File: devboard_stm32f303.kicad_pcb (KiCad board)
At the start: 2 copper layers, 50 x 17.8 mm, 20 parts, among them J2 USB_B_Mini, J3 Conn_01x20, J4 Conn_01x20, U1 STM32F303CCTx, U2 AMS1117-3.3, Y1 Crystal_Small

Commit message: More routing
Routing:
- net GND: track 45.2 -> 51.8 mm
- net +3V3: track 110.8 -> 117.0 mm
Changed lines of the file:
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@@
     (thickness 1.6)
     (drawings 9)
-    (tracks 194)
+    (tracks 202)
     (zones 0)
     (modules 20)
@@
   (segment (start 110.49 36.068) (end 107.315 32.893) (width 0.254) (layer B.Cu) (net 1))
   (segment (start 107.315 32.893) (end 107.331136 32.909136) (width 0.254) (layer B.Cu) (net 1))
+  (segment (start 97.0785 36.068) (end 97.566 36.068) (width 0.254) (layer F.Cu) (net 1))
+  (segment (start 96.498 36.068) (end 97.0785 36.068) (width 0.254) (layer F.Cu) (net 1))
+  (segment (start 93.091 32.661) (end 96.498 36.068) (width 0.254) (layer F.Cu) (net 1))
+  (segment (start 93.091 31.907) (end 93.091 32.661) (width 0.254) (layer F.Cu) (net 1))
   (segment (start 111.322 33.401) (end 112.649 33.401) (width 0.127) (layer F.Cu) (net 2))
   (segment (start 109.483675 35.239325) (end 111.322 33.401) (width 0.127) (layer F.Cu) (net 2))
@@
   (segment (start 96.266 32.193) (end 96.266 25.4) (width 0.254) (layer F.Cu) (net 4))
   (segment (start 96.266 25.4) (end 96.774 24.892) (width 0.254) (layer F.Cu) (net 4))
-  (segment (start 96.774 24.892) (end 99.314 24.892) (width 0.254) (layer F.Cu) (net 4))
   (segment (start 99.088628 24.893372) (end 99.314 24.892) (width 0.254) (layer F.Cu) (net 4))
   (segment (start 99.314 24.892) (end 113.539372 24.893372) (width 0.254) (layer F.Cu) (net 4))
@@
   (segment (start 111.76 27.686) (end 115.951 27.686) (width 0.254) (layer F.Cu) (net 4))
   (segment (start 116.205 27.432) (end 116.078 27.432) (width 0.254) (layer F.Cu) (net 4))
+  (segment (start 93.091 28.553) (end 96.752 24.892) (width 0.254) (layer F.Cu) (net 4))
+  (segment (start 93.091 29.307) (end 93.091 28.553) (width 0.254) (layer F.Cu) (net 4))
+  (segment (start 96.774 24.892) (end 97.028 24.892) (width 0.254) (layer F.Cu) (net 4))
+  (segment (start 96.752 24.892) (end 97.028 24.892) (width 0.254) (layer F.Cu) (net 4))
+  (segment (start 97.028 24.892) (end 99.314 24.892) (width 0.254) (layer F.Cu) (net 4))
   (via (at 108.458 35.802825) (size 0.6) (drill 0.3) (layers F.Cu B.Cu) (net 5))
   (segment (start 110.5685 36.068) (end 108.723175 36.068) (width 0.127) (layer F.Cu) (net 5))

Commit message: New board layout
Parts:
- C5: moved to F.Cu
- C8, D1, R2: moved to B.Cu
- moved C8 9.03 mm to (126.7, 26.2)
- moved C6 7.36 mm to (118.8, 37.1)
- moved R2 3.73 mm to (131.2, 30.2), turned to 0 degrees
- moved F1 3.37 mm to (131.2, 27.9), turned to 180 degrees
- moved J3 3.30 mm to (140.7, 20.3)
- moved D1 2.81 mm to (131.2, 32.5)
- moved C7 2.39 mm to (97.8, 24.1)
- moved C3 2.29 mm to (111.4, 24.1)
- moved J4 1.78 mm to (140.7, 40.6)
- moved C2 1.63 mm to (116.8, 28.8)
- moved C1 1.63 mm to (116.8, 32.4)
- moved Y1 1.62 mm to (113.9, 30.6)
- moved C9 0.91 mm to (126.7, 30.0), turned to 270 degrees
- moved U2 0.88 mm to (126.8, 30.0), turned to 180 degrees
- moved C4 0.85 mm to (98.1, 36.8)
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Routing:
- net +3V3: track 117.0 -> 0.00 mm, vias 3 -> 0
- net GND: track 51.8 -> 0.00 mm, vias 2 -> 0
- net D+: track 37.1 -> 0.00 mm, vias 4 -> 0
- net D-: track 35.6 -> 0.00 mm, vias 2 -> 0
- net OSC_OUT: track 12.8 -> 0.00 mm
- net OSC_IN: track 9.87 -> 0.00 mm
- net BOOT0: track 9.60 -> 0.00 mm, vias 3 -> 0
- net Net-(F1-Pad1): track 8.07 -> 0.00 mm, vias 1 -> 0
- net RESET: track 7.16 -> 0.00 mm, vias 2 -> 0
- net Net-(C8-Pad1): track 6.68 -> 0.00 mm
- net VBUS: track 3.11 -> 0.00 mm, vias 1 -> 0
- net Net-(JP1-Pad2): track 2.73 -> 0.00 mm, vias 1 -> 0
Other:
- board size 50 x 17.8 mm -> 51.1 x 22.4 mm
- net class Default: clearance 0.2 -> 0.127
- net class Power: clearance 0.2 -> 0.1905
- rule trace_clearance: 0.2 -> 0.127

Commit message: Basic routing
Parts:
- added D2: 1N5819, Diode_SMD:D_SOD-123, B.Cu at (137.8, 25.9)
- added SW1: SW_Push, Button_Switch_THT:SW_PUSH_6mm, F.Cu at (130.0, 37.0)
- C6: moved to B.Cu
- JP1: footprint Jumper:SolderJumper-3_P1.3mm_Open_Pad1.0x1.5mm -> Connector_PinHeader_2.54mm:PinHeader_1x03_P2.54mm_Vertical
- moved F1 9.21 mm to (140.1, 30.4), turned to 270 degrees
- moved D1 7.07 mm to (137.8, 35.1)
- moved C5 6.63 mm to (112.9, 30.4)
- moved C6 6.13 mm to (124.5, 34.7)
- moved C8 6.01 mm to (132.3, 24.0), turned to 270 degrees
- moved Y1 4.62 mm to (114.6, 35.1)
- moved C2 4.62 mm to (117.5, 33.4)
- moved C1 4.62 mm to (117.5, 37.0)
- moved U2 4.06 mm to (126.8, 25.9)
- moved C9 4.06 mm to (126.7, 25.9)
- moved JP1 3.18 mm to (93.2, 33.8), turned to 180 degrees
- moved R2 2.58 mm to (132.3, 27.9), turned to 270 degrees
- moved R1 0.76 mm to (96.3, 30.8)
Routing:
- net +3V3: track 0.00 -> 75.8 mm, vias 0 -> 4
- net D+: track 0.00 -> 56.5 mm
- net D-: track 0.00 -> 55.4 mm
- net GND: track 0.00 -> 30.1 mm, vias 0 -> 2
- net OSC_OUT: track 0.00 -> 13.7 mm
- net OSC_IN: track 0.00 -> 12.2 mm

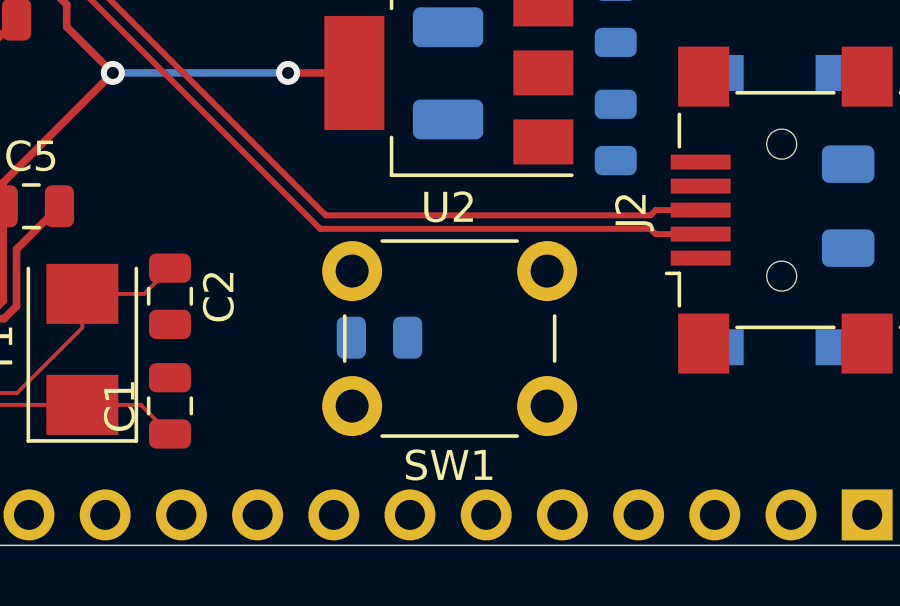
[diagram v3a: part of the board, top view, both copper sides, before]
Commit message: Autoroute rest of the board
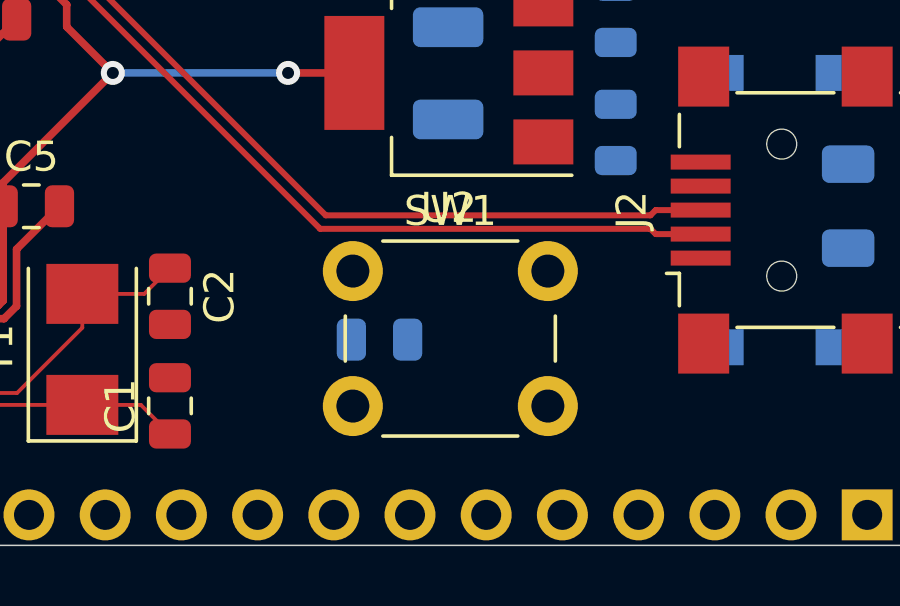
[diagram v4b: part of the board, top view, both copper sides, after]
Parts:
- moved SW1 7.89 mm to (123.6, 32.5), turned to 0 degrees
- moved C6 0.06 mm to (124.5, 34.8)
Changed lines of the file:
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@@
   )
   (module Button_Switch_THT:SW_PUSH_6mm (layer F.Cu)
-    (at 130.048 37.012 180)
+    (at 123.571 32.512)
     (descr https://www.omron.com/ecb/products/pdf/en-b3f.pdf)
     (tags "tact sw push 6mm")
@@
       (effects (font (size 1 1) (thickness 0.15)))
     )
-    (pad 1 thru_hole circle (at 6.5 0 270) (size 2 2) (drill 1.1) (layers *.Cu *.Mask)
-      (net 1 GND))
-    (pad 2 thru_hole circle (at 6.5 4.5 270) (size 2 2) (drill 1.1) (layers *.Cu *.Mask)
+    (pad 1 thru_hole circle (at 6.5 0 90) (size 2 2) (drill 1.1) (layers *.Cu *.Mask)
+      (net 1 GND))
+    (pad 2 thru_hole circle (at 6.5 4.5 90) (size 2 2) (drill 1.1) (layers *.Cu *.Mask)
       (net 5 RESET))
-    (pad 1 thru_hole circle (at 0 0 270) (size 2 2) (drill 1.1) (layers *.Cu *.Mask)
-      (net 1 GND))
-    (pad 2 thru_hole circle (at 0 4.5 270) (size 2 2) (drill 1.1) (layers *.Cu *.Mask)
+    (pad 1 thru_hole circle (at 0 0 90) (size 2 2) (drill 1.1) (layers *.Cu *.Mask)
+      (net 1 GND))
+    (pad 2 thru_hole circle (at 0 4.5 90) (size 2 2) (drill 1.1) (layers *.Cu *.Mask)
       (net 5 RESET))
     (model ${KISYS3DMOD}/Button_Switch_THT.3dshapes/SW_PUSH_6mm.wrl
@@
   )
   (module Capacitor_SMD:C_0805_2012Metric (layer B.Cu)
-    (at 124.46 34.7345)
+    (at 124.46 34.798)
     (descr "Capacitor SMD 0805 (2012 Metric), square (rectangular) end terminal, IPC_7351 nominal, (Body size source: https://docs.google.com/spreadsheets/d/1BsfQQcO9C6DZCsRaXUlFlo91Tg2WpOkGARC1WS5S8t0/edit?usp=sharing), generated with kicad-footprint-generator")
     (tags capacitor)

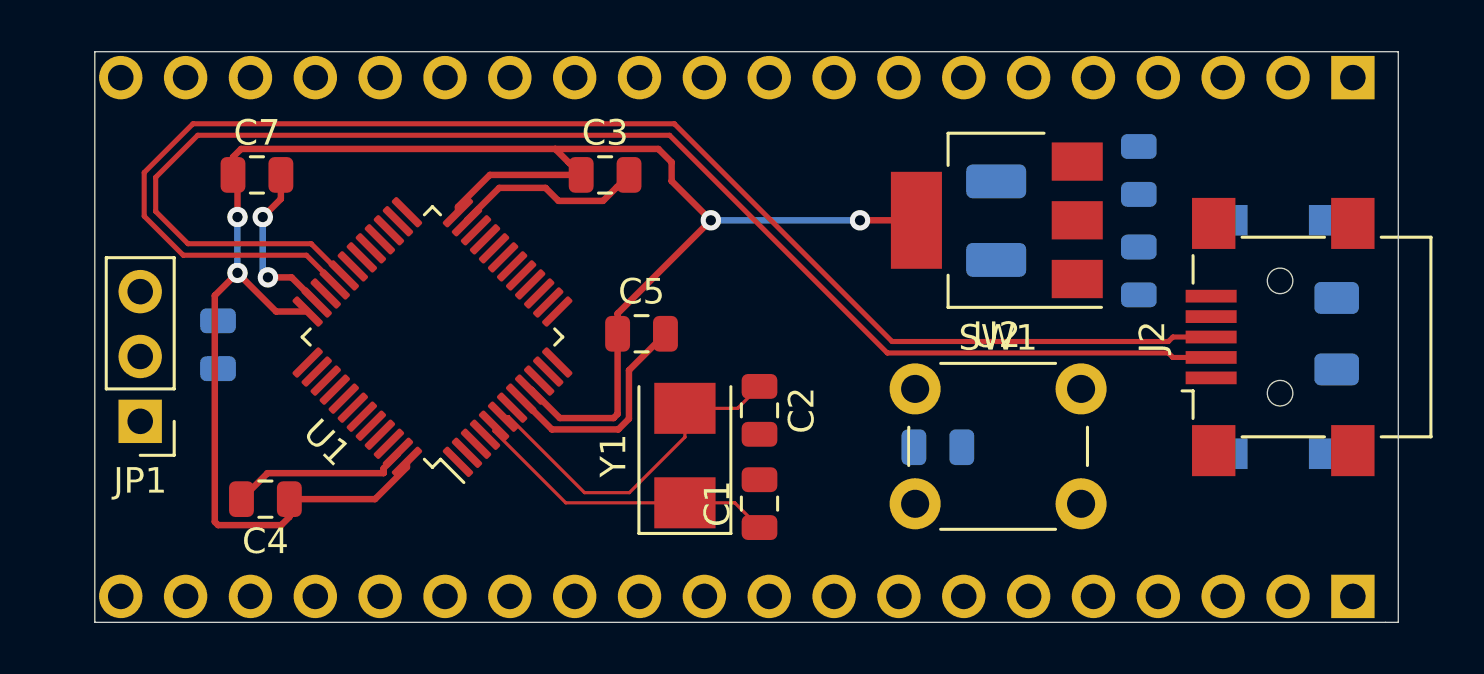
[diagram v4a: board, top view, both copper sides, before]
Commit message: Add ground fills
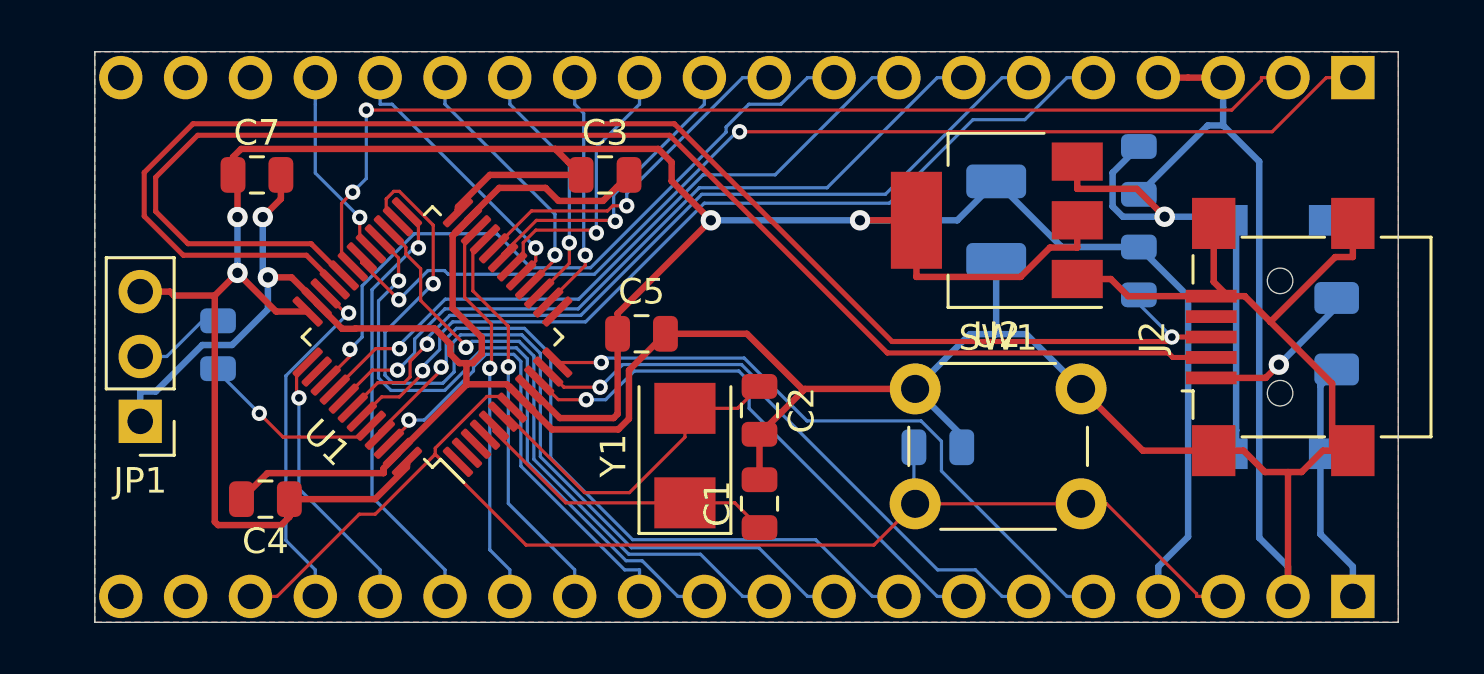
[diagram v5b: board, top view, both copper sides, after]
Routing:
- net GND: track 30.1 -> 157.7 mm
- net RESET: track 0.00 -> 50.6 mm
- net PA10: track 0.00 -> 43.4 mm, vias 0 -> 2
- net PA9: track 0.00 -> 43.4 mm, vias 0 -> 2
- net +3V3: track 75.8 -> 116.6 mm
- net PB13: track 0.00 -> 36.1 mm, vias 0 -> 1
- net PB7: track 0.00 -> 34.7 mm, vias 0 -> 1
- net PB6: track 0.00 -> 32.3 mm, vias 0 -> 1
- net PB5: track 0.00 -> 29.8 mm, vias 0 -> 1
- net PB8: track 0.00 -> 29.5 mm, vias 0 -> 1
- net PB3: track 0.00 -> 27.4 mm, vias 0 -> 1
- net PB4: track 0.00 -> 27.2 mm, vias 0 -> 1
- net PB15: track 0.00 -> 26.2 mm, vias 0 -> 1
- net PA2: track 0.00 -> 25.6 mm, vias 0 -> 1
- net PB14: track 0.00 -> 24.3 mm, vias 0 -> 1
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- added copper zone on B.Cu, net GND
- added copper zone on F.Cu, net GND
